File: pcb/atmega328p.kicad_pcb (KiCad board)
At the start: 2 copper layers, 40 x 60 mm, 24 parts, among them J1 Arduini MINI Left, J10 Buttons, J11 I2C, J2 Power, J3 Arduini MINI Right, J4 Hall Sensor, J5 Room Temperature, J6 Outlet Temperature, J7 Motor, J8 Glow Plug, J9 Oil Pump

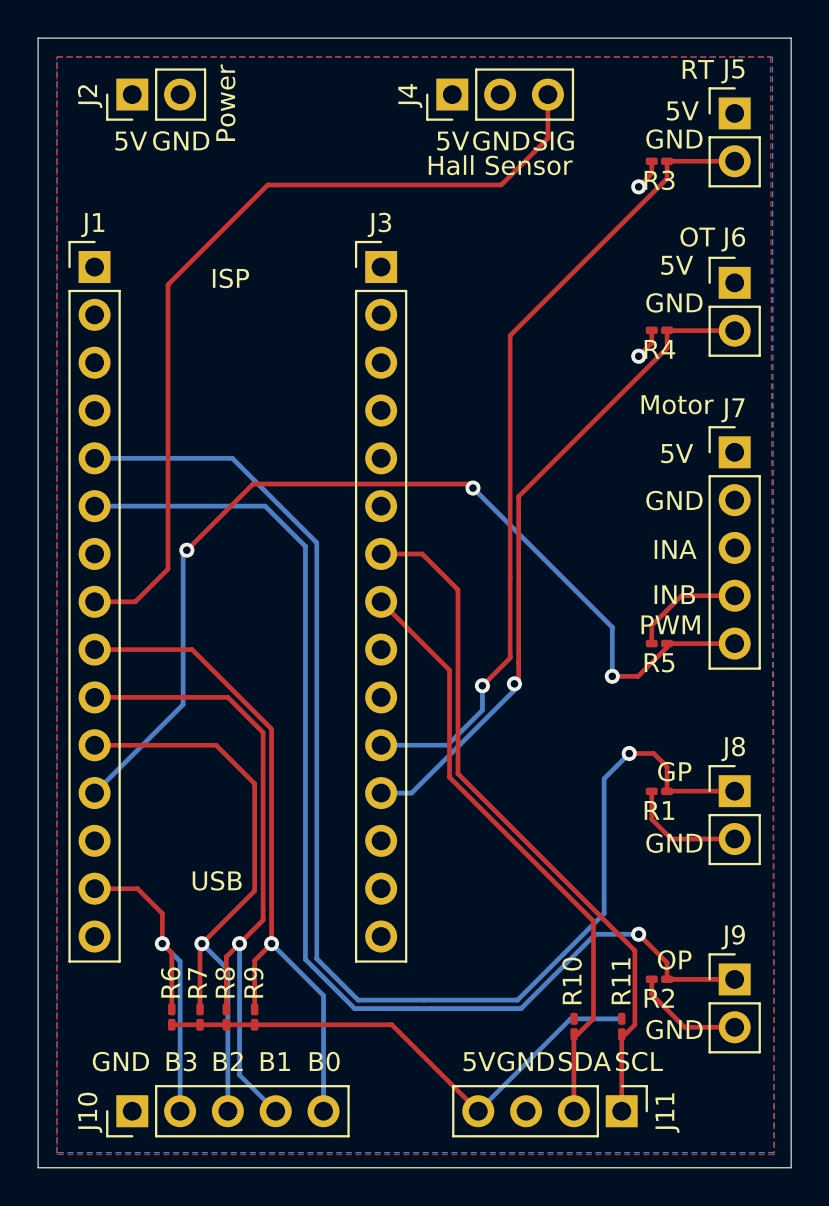
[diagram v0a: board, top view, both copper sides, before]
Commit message: added batter power adc
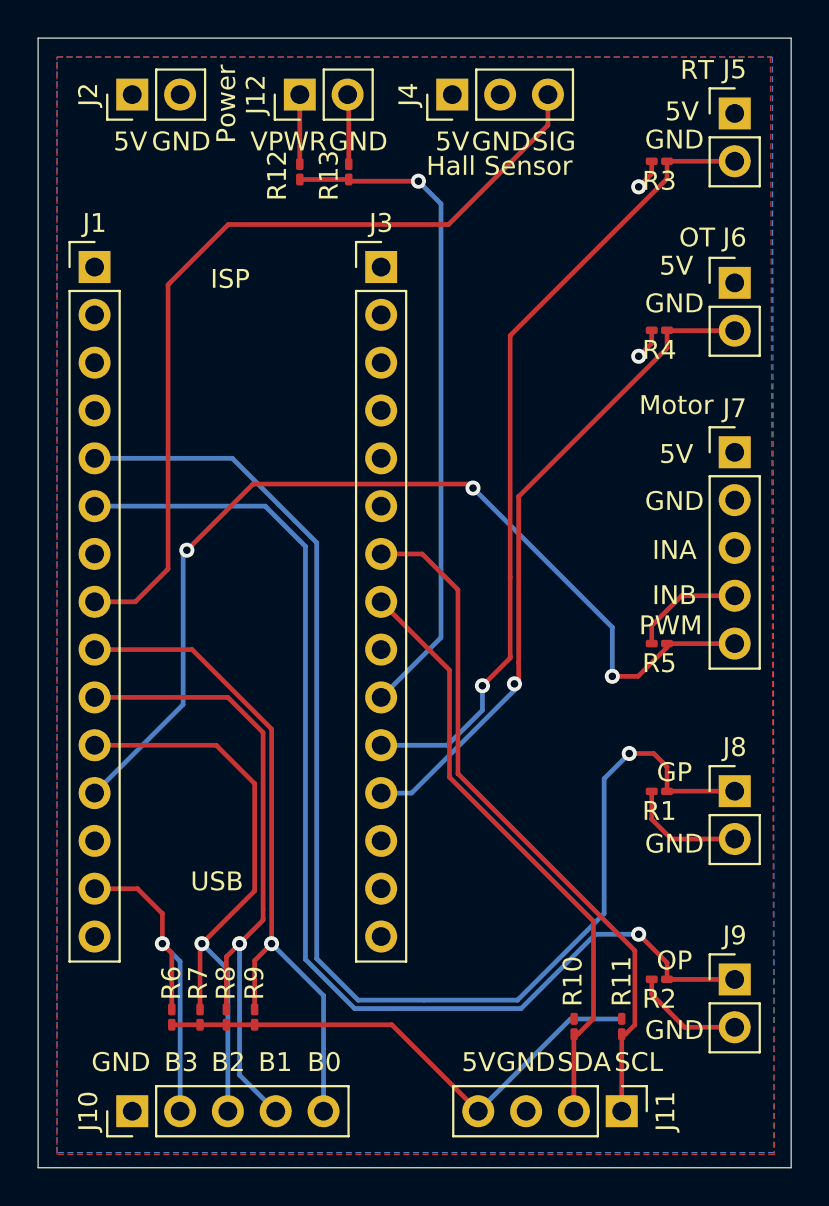
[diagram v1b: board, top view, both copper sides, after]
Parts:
- added J12: Power, Connector_PinHeader_2.54mm:PinHeader_1x02_P2.54mm_Vertical, F.Cu at (73.9, 43.0)
- added R12: 6.8K, Resistor_SMD:R_0201_0603Metric_Pad0.64x0.40mm_HandSolder, F.Cu at (73.9, 47.1)
- added R13: 3.3K, Resistor_SMD:R_0201_0603Metric_Pad0.64x0.40mm_HandSolder, F.Cu at (76.5, 47.1)
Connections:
- J3 pad 10: Net-(J3-Pad10) -> /VPWR
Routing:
- net /VPWR: track 0.00 -> 35.6 mm, vias 0 -> 1
- net GND: track 21.6 -> 25.3 mm
- net /12V: track 0.00 -> 3.69 mm
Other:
- board text added: "VPWR"
